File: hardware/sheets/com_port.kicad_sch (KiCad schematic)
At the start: 16 parts, among them J1 DE9_Pins, J2 Conn_01x03, J3 Conn_01x04, U1 16550, U2 MAX3241, U3 74HC04, U4 74HC08, U5 74HC08, U6 74HC125

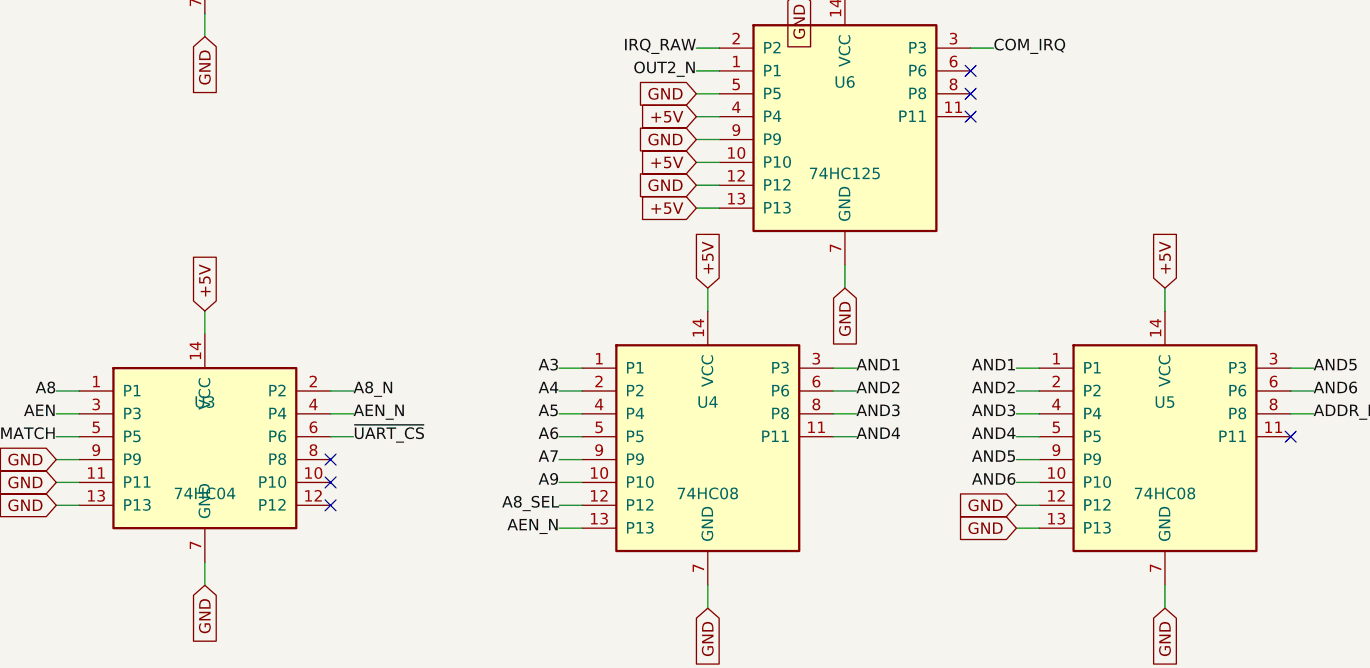
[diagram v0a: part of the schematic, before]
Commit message: Standardize 5V glue on 74HCT; fix bus-latch family; div-3 -> 74HCT163
All 5V 74-series logic moved from mixed HC/HCT to 74HCT (TTL thresholds reliably
read 3.3V level-shifter outputs). Fixes the address latches / data transceiver
that were wrongly 74HC instead of the design's 74HCT. The div-by-3 moves from
74HC4017 (no HCT variant) to a 74HCT163 preset-to-3 with a spare 74HCT04 gate
for the TC->~PE reload. Per-card level shifters use a dedicated 74LVC245A symbol.
Pinouts unchanged; netlist intact; zero structural ERC errors.

Co-Authored-By: Claude Opus 4.8 (1M context) <noreply@anthropic.com>
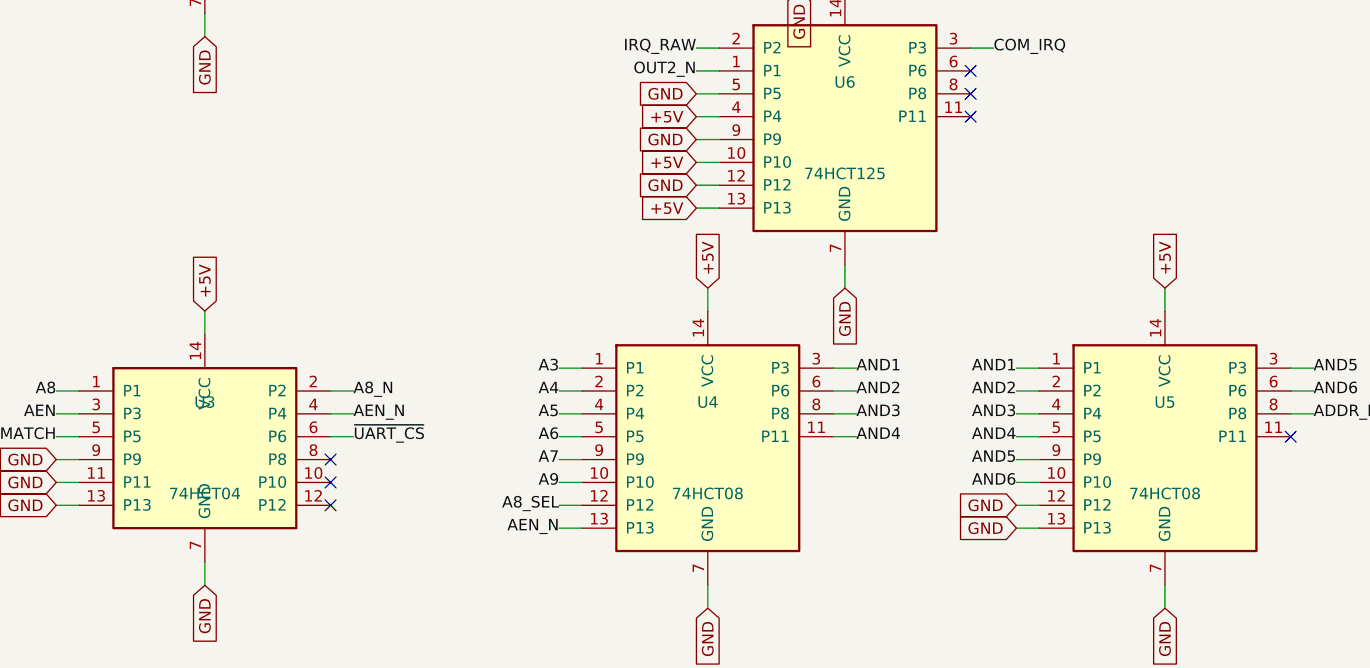
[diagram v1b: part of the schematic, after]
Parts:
- removed U3: 74HC04, symbol mini-xt:74HC04
- removed U4, U5: 74HC08, symbol mini-xt:74HC08
- removed U6: 74HC125, symbol mini-xt:74HC125
- added U3: 74HCT04, symbol mini-xt:74HCT04
- added U4, U5: 74HCT08, symbol mini-xt:74HCT08
- added U6: 74HCT125, symbol mini-xt:74HCT125
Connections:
- net +5V: now also U3.14 (VCC), U4.14 (VCC), U5.14 (VCC), U6.10 (P10), U6.13 (P13), U6.14 (VCC), U6.4 (P4)
- net A3: now also U4.1 (P1)
- net A4: now also U4.2 (P2)
- net A5: now also U4.4 (P4)
- net A6: now also U4.5 (P5)
- net A7: now also U4.9 (P9)
- net A8: now also U3.1 (P1)
- net A8_N: now also U3.2 (P2)
- net A8_SEL: now also U4.12 (P12)
- net A9: now also U4.10 (P10)
- net ADDR_MATCH: now also U3.5 (P5), U5.8 (P8)
- net AEN: now also U3.3 (P3)
- net AEN_N: now also U3.4 (P4), U4.13 (P13)
- net AND1: now also U4.3 (P3), U5.1 (P1)
- net AND2: now also U4.6 (P6), U5.2 (P2)
- net AND3: now also U4.8 (P8), U5.4 (P4)
- net AND4: now also U4.11 (P11), U5.5 (P5)
- net AND5: now also U5.3 (P3), U5.9 (P9)
- net AND6: now also U5.10 (P10), U5.6 (P6)
- net COM_IRQ: now also U6.3 (P3)
- net GND: now also U3.11 (P11), U3.13 (P13), U3.7 (GND), U3.9 (P9), U4.7 (GND), U5.12 (P12), U5.13 (P13), U5.7 (GND), U6.12 (P12), U6.5 (P5), U6.7 (GND), U6.9 (P9)
- net IRQ_RAW: now also U6.2 (P2)
- net OUT2_N: now also U6.1 (P1)
- net ~{UART_CS}: now also U3.6 (P6)
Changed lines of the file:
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@@
 		(instances
 			(project "mini-xt"
-				(path "/d5fb706d-3720-437f-850e-91a8fdce298f/7e9cd34f-5121-4f1c-a33e-91087b9717c1"
+				(path "/12a90590-121b-4b08-bc73-62c223de1072/c12b9b45-b925-431d-82a4-2ca3dd335cbf"
 					(reference "U501")
 					(unit 1)
 				)
-				(path "/d5fb706d-3720-437f-850e-91a8fdce298f/03a0a081-b4c2-4aa3-9929-4e36c4bfe197"
+				(path "/12a90590-121b-4b08-bc73-62c223de1072/664d93ef-1dfb-4787-8b08-6831b31c9b8e"
 					(reference "U601")
 					(unit 1)
@@
 		(instances
 			(project "mini-xt"
-				(path "/d5fb706d-3720-437f-850e-91a8fdce298f/7e9cd34f-5121-4f1c-a33e-91087b9717c1"
+				(path "/12a90590-121b-4b08-bc73-62c223de1072/c12b9b45-b925-431d-82a4-2ca3dd335cbf"
 					(reference "OSC501")
 					(unit 1)
 				)
-				(path "/d5fb706d-3720-437f-850e-91a8fdce298f/03a0a081-b4c2-4aa3-9929-4e36c4bfe197"
+				(path "/12a90590-121b-4b08-bc73-62c223de1072/664d93ef-1dfb-4787-8b08-6831b31c9b8e"
 					(reference "OSC601")
 					(unit 1)
@@
 	)
 	(symbol
-		(lib_id "mini-xt:74HC04")
+		(lib_id "mini-xt:74HCT04")
 		(at 60.96 198.12 0)
 		(unit 1)
@@
 			)
 		)
-		(property "Value" "74HC04"
+		(property "Value" "74HCT04"
 			(at 60.96 203.2 0)
 			(effects
@@
 		(instances
 			(project "mini-xt"
-				(path "/d5fb706d-3720-437f-850e-91a8fdce298f/7e9cd34f-5121-4f1c-a33e-91087b9717c1"
+				(path "/12a90590-121b-4b08-bc73-62c223de1072/c12b9b45-b925-431d-82a4-2ca3dd335cbf"
 					(reference "U503")
 					(unit 1)
 				)
-				(path "/d5fb706d-3720-437f-850e-91a8fdce298f/03a0a081-b4c2-4aa3-9929-4e36c4bfe197"
+				(path "/12a90590-121b-4b08-bc73-62c223de1072/664d93ef-1dfb-4787-8b08-6831b31c9b8e"
 					(reference "U603")
 					(unit 1)
@@
 		(instances
 			(project "mini-xt"
-				(path "/d5fb706d-3720-437f-850e-91a8fdce298f/7e9cd34f-5121-4f1c-a33e-91087b9717c1"
+				(path "/12a90590-121b-4b08-bc73-62c223de1072/c12b9b45-b925-431d-82a4-2ca3dd335cbf"
 					(reference "J502")
 					(unit 1)
 				)
-				(path "/d5fb706d-3720-437f-850e-91a8fdce298f/03a0a081-b4c2-4aa3-9929-4e36c4bfe197"
+				(path "/12a90590-121b-4b08-bc73-62c223de1072/664d93ef-1dfb-4787-8b08-6831b31c9b8e"
 					(reference "J602")
 					(unit 1)
@@
 	)
 	(symbol
-		(lib_id "mini-xt:74HC08")
+		(lib_id "mini-xt:74HCT08")
 		(at 116.84 198.12 0)
 		(unit 1)
@@
 			)
 		)
-		(property "Value" "74HC08"
+		(property "Value" "74HCT08"
 			(at 116.84 203.2 0)
 			(effects
@@
 		(instances
 			(project "mini-xt"
-				(path "/d5fb706d-3720-437f-850e-91a8fdce298f/7e9cd34f-5121-4f1c-a33e-91087b9717c1"
+				(path "/12a90590-121b-4b08-bc73-62c223de1072/c12b9b45-b925-431d-82a4-2ca3dd335cbf"
 					(reference "U504")
 					(unit 1)
 				)
-				(path "/d5fb706d-3720-437f-850e-91a8fdce298f/03a0a081-b4c2-4aa3-9929-4e36c4bfe197"
+				(path "/12a90590-121b-4b08-bc73-62c223de1072/664d93ef-1dfb-4787-8b08-6831b31c9b8e"
 					(reference "U604")
 					(unit 1)
@@
 	)
 	(symbol
-		(lib_id "mini-xt:74HC08")
+		(lib_id "mini-xt:74HCT08")
 		(at 167.64 198.12 0)
 		(unit 1)
@@
 			)
 		)
-		(property "Value" "74HC08"
+		(property "Value" "74HCT08"
 			(at 167.64 203.2 0)
 			(effects
@@
 		(instances
 			(project "mini-xt"
-				(path "/d5fb706d-3720-437f-850e-91a8fdce298f/7e9cd34f-5121-4f1c-a33e-91087b9717c1"
+				(path "/12a90590-121b-4b08-bc73-62c223de1072/c12b9b45-b925-431d-82a4-2ca3dd335cbf"
 					(reference "U505")
 					(unit 1)
 				)
-				(path "/d5fb706d-3720-437f-850e-91a8fdce298f/03a0a081-b4c2-4aa3-9929-4e36c4bfe197"
+				(path "/12a90590-121b-4b08-bc73-62c223de1072/664d93ef-1dfb-4787-8b08-6831b31c9b8e"
 					(reference "U605")
 					(unit 1)
@@
 	)
 	(symbol
-		(lib_id "mini-xt:74HC125")
+		(lib_id "mini-xt:74HCT125")
 		(at 132.08 162.56 0)
 		(unit 1)
@@
 			)
 		)
-		(property "Value" "74HC125"
+		(property "Value" "74HCT125"
 			(at 132.08 167.64 0)
 			(effects
@@
 		(instances
 			(project "mini-xt"
-				(path "/d5fb706d-3720-437f-850e-91a8fdce298f/7e9cd34f-5121-4f1c-a33e-91087b9717c1"
+				(path "/12a90590-121b-4b08-bc73-62c223de1072/c12b9b45-b925-431d-82a4-2ca3dd335cbf"
 					(reference "U506")
 					(unit 1)
 				)
-				(path "/d5fb706d-3720-437f-850e-91a8fdce298f/03a0a081-b4c2-4aa3-9929-4e36c4bfe197"
+				(path "/12a90590-121b-4b08-bc73-62c223de1072/664d93ef-1dfb-4787-8b08-6831b31c9b8e"
 					(reference "U606")
 					(unit 1)
@@
 		(instances
 			(project "mini-xt"
-				(path "/d5fb706d-3720-437f-850e-91a8fdce298f/7e9cd34f-5121-4f1c-a33e-91087b9717c1"
+				(path "/12a90590-121b-4b08-bc73-62c223de1072/c12b9b45-b925-431d-82a4-2ca3dd335cbf"
 					(reference "U502")
 					(unit 1)
 				)
-				(path "/d5fb706d-3720-437f-850e-91a8fdce298f/03a0a081-b4c2-4aa3-9929-4e36c4bfe197"
+				(path "/12a90590-121b-4b08-bc73-62c223de1072/664d93ef-1dfb-4787-8b08-6831b31c9b8e"
 					(reference "U602")
 					(unit 1)
@@
 		(instances
 			(project "mini-xt"
-				(path "/d5fb706d-3720-437f-850e-91a8fdce298f/7e9cd34f-5121-4f1c-a33e-91087b9717c1"
+				(path "/12a90590-121b-4b08-bc73-62c223de1072/c12b9b45-b925-431d-82a4-2ca3dd335cbf"
 					(reference "C503")
 					(unit 1)
 				)
-				(path "/d5fb706d-3720-437f-850e-91a8fdce298f/03a0a081-b4c2-4aa3-9929-4e36c4bfe197"
+				(path "/12a90590-121b-4b08-bc73-62c223de1072/664d93ef-1dfb-4787-8b08-6831b31c9b8e"
 					(reference "C603")
 					(unit 1)
@@
 		(instances
 			(project "mini-xt"
-				(path "/d5fb706d-3720-437f-850e-91a8fdce298f/7e9cd34f-5121-4f1c-a33e-91087b9717c1"
+				(path "/12a90590-121b-4b08-bc73-62c223de1072/c12b9b45-b925-431d-82a4-2ca3dd335cbf"
 					(reference "C504")
 					(unit 1)
 				)
-				(path "/d5fb706d-3720-437f-850e-91a8fdce298f/03a0a081-b4c2-4aa3-9929-4e36c4bfe197"
+				(path "/12a90590-121b-4b08-bc73-62c223de1072/664d93ef-1dfb-4787-8b08-6831b31c9b8e"
 					(reference "C604")
 					(unit 1)
@@
 		(instances
 			(project "mini-xt"
-				(path "/d5fb706d-3720-437f-850e-91a8fdce298f/7e9cd34f-5121-4f1c-a33e-91087b9717c1"
+				(path "/12a90590-121b-4b08-bc73-62c223de1072/c12b9b45-b925-431d-82a4-2ca3dd335cbf"
 					(reference "C505")
 					(unit 1)
 				)
-				(path "/d5fb706d-3720-437f-850e-91a8fdce298f/03a0a081-b4c2-4aa3-9929-4e36c4bfe197"
+				(path "/12a90590-121b-4b08-bc73-62c223de1072/664d93ef-1dfb-4787-8b08-6831b31c9b8e"
 					(reference "C605")
 					(unit 1)
@@
 		(instances
 			(project "mini-xt"
-				(path "/d5fb706d-3720-437f-850e-91a8fdce298f/7e9cd34f-5121-4f1c-a33e-91087b9717c1"
+				(path "/12a90590-121b-4b08-bc73-62c223de1072/c12b9b45-b925-431d-82a4-2ca3dd335cbf"
 					(reference "C506")
 					(unit 1)
 				)
-				(path "/d5fb706d-3720-437f-850e-91a8fdce298f/03a0a081-b4c2-4aa3-9929-4e36c4bfe197"
+				(path "/12a90590-121b-4b08-bc73-62c223de1072/664d93ef-1dfb-4787-8b08-6831b31c9b8e"
 					(reference "C606")
 					(unit 1)
@@
 		(instances
 			(project "mini-xt"
-				(path "/d5fb706d-3720-437f-850e-91a8fdce298f/7e9cd34f-5121-4f1c-a33e-91087b9717c1"
+				(path "/12a90590-121b-4b08-bc73-62c223de1072/c12b9b45-b925-431d-82a4-2ca3dd335cbf"
 					(reference "J501")
 					(unit 1)
 				)
-				(path "/d5fb706d-3720-437f-850e-91a8fdce298f/03a0a081-b4c2-4aa3-9929-4e36c4bfe197"
+				(path "/12a90590-121b-4b08-bc73-62c223de1072/664d93ef-1dfb-4787-8b08-6831b31c9b8e"
 					(reference "J601")
 					(unit 1)
@@
 		(instances
 			(project "mini-xt"
-				(path "/d5fb706d-3720-437f-850e-91a8fdce298f/7e9cd34f-5121-4f1c-a33e-91087b9717c1"
+				(path "/12a90590-121b-4b08-bc73-62c223de1072/c12b9b45-b925-431d-82a4-2ca3dd335cbf"
 					(reference "J503")
 					(unit 1)
 				)
-				(path "/d5fb706d-3720-437f-850e-91a8fdce298f/03a0a081-b4c2-4aa3-9929-4e36c4bfe197"
+				(path "/12a90590-121b-4b08-bc73-62c223de1072/664d93ef-1dfb-4787-8b08-6831b31c9b8e"
 					(reference "J603")
 					(unit 1)
@@
 		(instances
 			(project "mini-xt"
-				(path "/d5fb706d-3720-437f-850e-91a8fdce298f/7e9cd34f-5121-4f1c-a33e-91087b9717c1"
+				(path "/12a90590-121b-4b08-bc73-62c223de1072/c12b9b45-b925-431d-82a4-2ca3dd335cbf"
 					(reference "C501")
 					(unit 1)
 				)
-				(path "/d5fb706d-3720-437f-850e-91a8fdce298f/03a0a081-b4c2-4aa3-9929-4e36c4bfe197"
+				(path "/12a90590-121b-4b08-bc73-62c223de1072/664d93ef-1dfb-4787-8b08-6831b31c9b8e"
 					(reference "C601")
 					(unit 1)
@@
 		(instances
 			(project "mini-xt"
-				(path "/d5fb706d-3720-437f-850e-91a8fdce298f/7e9cd34f-5121-4f1c-a33e-91087b9717c1"
+				(path "/12a90590-121b-4b08-bc73-62c223de1072/c12b9b45-b925-431d-82a4-2ca3dd335cbf"
 					(reference "C502")
 					(unit 1)
 				)
-				(path "/d5fb706d-3720-437f-850e-91a8fdce298f/03a0a081-b4c2-4aa3-9929-4e36c4bfe197"
+				(path "/12a90590-121b-4b08-bc73-62c223de1072/664d93ef-1dfb-4787-8b08-6831b31c9b8e"
 					(reference "C602")
 					(unit 1)
